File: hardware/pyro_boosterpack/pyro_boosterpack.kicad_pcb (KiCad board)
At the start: 2 copper layers, 50.8 x 35.6 mm, 7 parts, among them J1 Conn_01x02, J2 Conn_01x08, J3 Conn_01x40, Q1 Q_NMOS_GSD, Q2 Q_NMOS_GSD, Q3 Q_NMOS_GSD, Q4 Q_NMOS_GSD

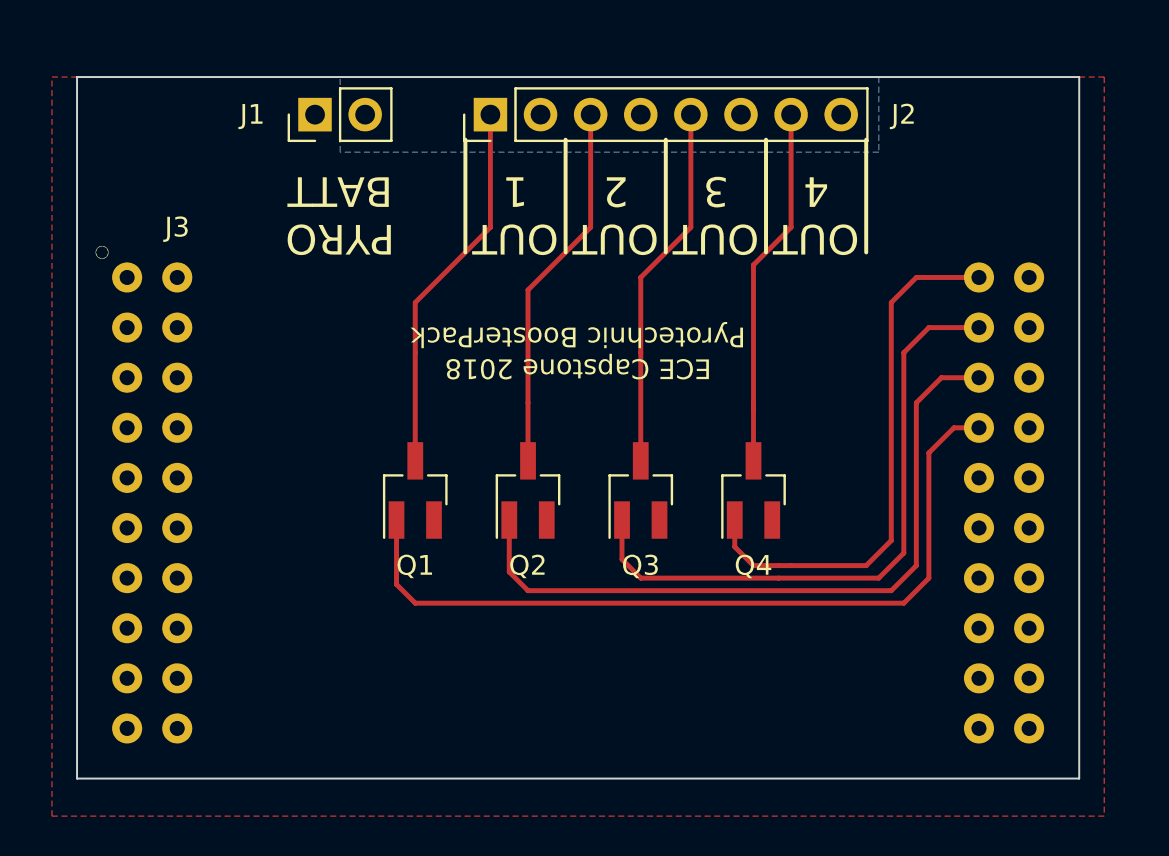
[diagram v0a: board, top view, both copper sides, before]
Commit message: Added INA260 to pyro board
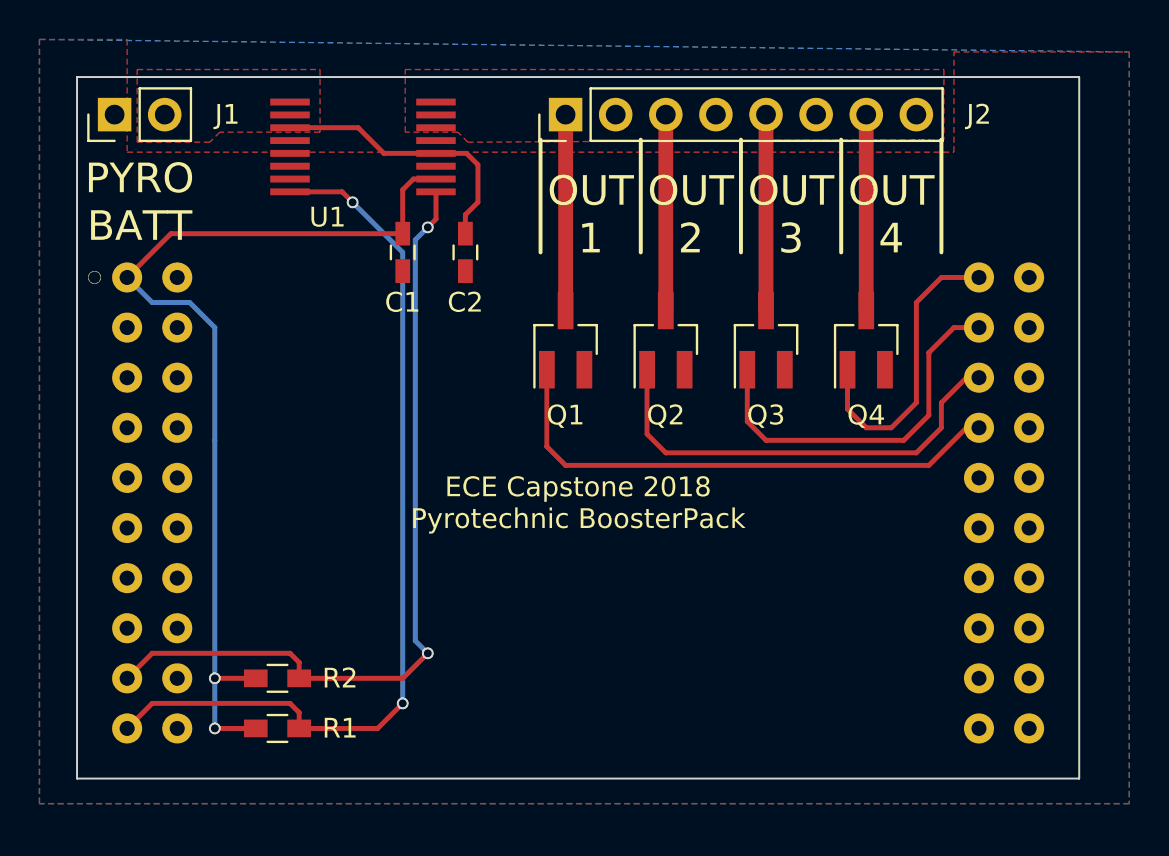
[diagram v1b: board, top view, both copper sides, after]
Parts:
- added C1: 0.1uF, Capacitors_SMD:C_0603_HandSoldering, F.Cu at (141.0, 101.6)
- added C2: 0.1uF, Capacitors_SMD:C_0603_HandSoldering, F.Cu at (144.1, 101.6)
- added R1: 4.7k, Resistors_SMD:R_0603_HandSoldering, F.Cu at (134.6, 125.7)
- added R2: 4.7k, Resistors_SMD:R_0603_HandSoldering, F.Cu at (134.6, 123.2)
- added U1: ina260, capstone_board_components:tssop-16, F.Cu at (135.3, 94.0)
- moved Q1 10.8 mm to (149.2, 106.0)
- moved Q2 10.3 mm to (154.3, 106.0)
- moved J1 10.2 mm to (126.4, 94.6)
- moved Q3 9.92 mm to (159.4, 106.0)
- moved Q4 9.53 mm to (164.5, 106.0)
- moved J2 3.81 mm to (149.2, 94.6)
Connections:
- J2 pad 2: +BATT -> /BATT_LOAD
- J2 pad 4: +BATT -> /BATT_LOAD
- J2 pad 6: +BATT -> /BATT_LOAD
- J2 pad 8: +BATT -> /BATT_LOAD
- J3 pad 1: Net-(J3-Pad1) -> +3V3
- J3 pad 10: Net-(J3-Pad10) -> /SDA
- J3 pad 9: Net-(J3-Pad9) -> /SCL
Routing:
- net +3V3: track 0.00 -> 49.3 mm, vias 0 -> 2
- net /SDA: track 0.00 -> 45.9 mm, vias 0 -> 2
- net /SCL: track 0.00 -> 41.4 mm, vias 0 -> 2
- net /PYRO_1_EN: track 40.6 -> 26.4 mm
- net +BATT: track 0.00 -> 14.1 mm
- net /PYRO_2_EN: track 36.8 -> 23.4 mm
- net /PYRO_3_EN: track 31.7 -> 19.0 mm
- net /PYRO_4_EN: track 27.3 -> 15.2 mm
- net /PYRO_1_OUT: track 19.1 -> 9.93 mm
- net /PYRO_2_OUT: track 18.9 -> 9.93 mm
- net /PYRO_4_OUT: track 18.7 -> 9.93 mm
- net /PYRO_3_OUT: track 18.6 -> 9.93 mm
- added copper zone on F.Cu, net +BATT
- added copper zone on F.Cu, net /BATT_LOAD
- added copper zone on B.Cu, net GND
- removed copper zone on B.Cu, net +BATT

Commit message: Fixed hole sizes (ugh)
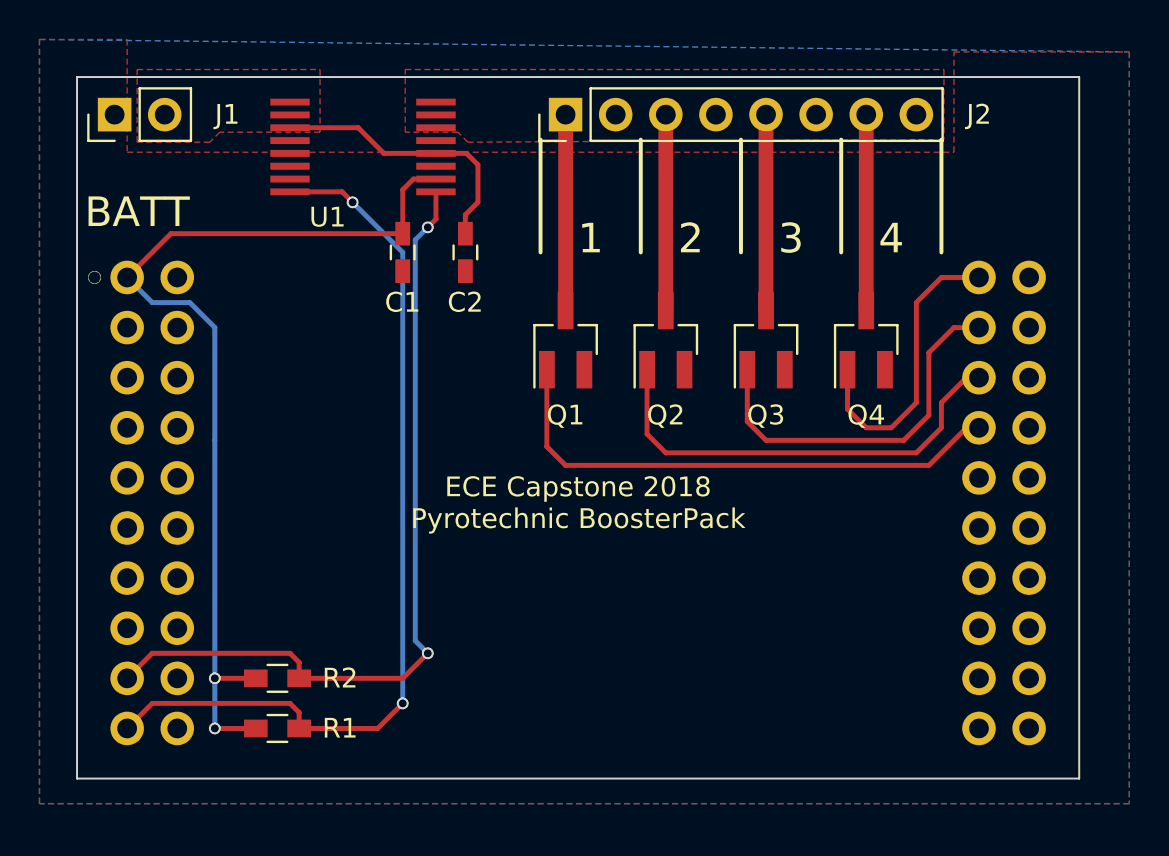
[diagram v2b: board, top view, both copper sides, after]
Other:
- board text added: "1"
- board text added: "2"
- board text added: "3"
- board text added: "4"
- board text added: "Ag Despopoulos Version 2"
- board text added: "BATT"
- board text removed: "Ag Despopoulos Version 1"
- board text removed: "OUT 1"
- board text removed: "OUT 2"
- board text removed: "OUT 3"
- board text removed: "OUT 4"
- board text removed: "PYRO BATT"
